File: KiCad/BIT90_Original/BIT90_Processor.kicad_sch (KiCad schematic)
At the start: 24 parts, among them SW65 RST, U1 D4016, U13 74LS138, U14 74LS05, U2 2764, U3 2764, U4 2764, U5 Z80, U6 74LS74, U8 74LS32

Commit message: Completed original schematic redraw
Well, didn't finish the Video Encoder (PAL) sheet as I'm not going to use any of it in the new design.
Moved the audio output from that sheet to the Joystick/Audio/Tape out sheet where the sound generator is.
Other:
- moved on the sheet: C15, C76, D2, D3, D4, R1, R10, R11, R21, R22, R35, R39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

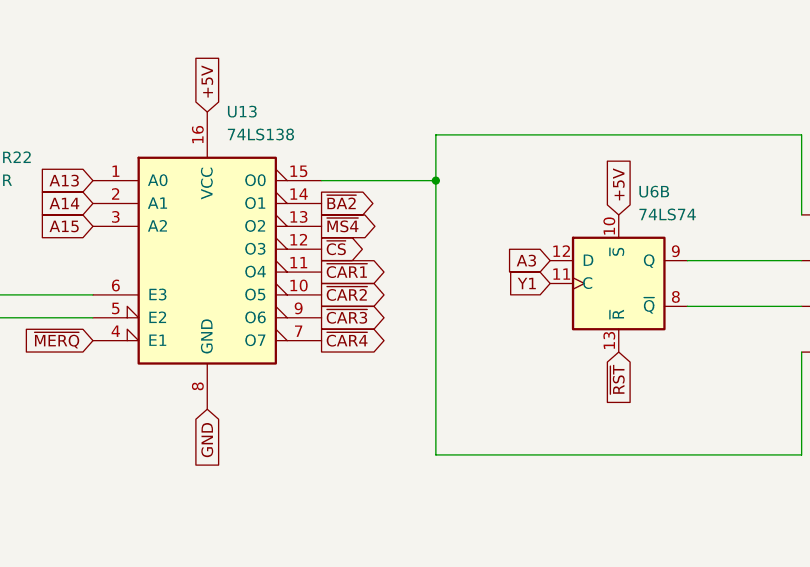
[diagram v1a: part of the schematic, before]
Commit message: Small updates/corrections
Managed to figure out some more errors/missing info from ColecoVision schematics & Henk's BIT90 motherboard underside photo
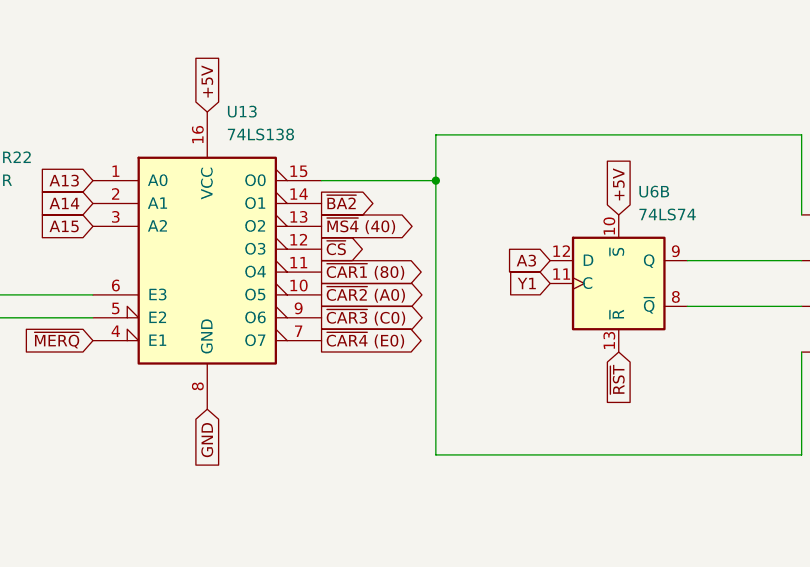
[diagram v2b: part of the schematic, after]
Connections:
- net ~{CAR1} renamed ~{CAR1} (80)
- net ~{CAR2} renamed ~{CAR2} (A0)
- net ~{CAR3} renamed ~{CAR3} (C0)
- net ~{CAR4} renamed ~{CAR4} (E0)
- net ~{MS4} renamed ~{MS4} (40)
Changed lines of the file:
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@@
 	(title_block
 		(title "BIT90 Processor")
-		(date "4/JUN/2026")
+		(date "5/JUN/2026")
 		(rev "A")
 		(company "Brett Hallen")
@@
 		)
 	)
-	(global_label "~{CAR1}"
+	(global_label "~{CAR1} (80)"
 		(shape output)
 		(at 102.87 57.15 0)
@@
 		)
 	)
-	(global_label "~{CAR3}"
+	(global_label "~{CAR3} (C0)"
 		(shape output)
 		(at 102.87 62.23 0)
@@
 		)
 	)
-	(global_label "~{MS4}"
+	(global_label "~{MS4} (40)"
 		(shape output)
 		(at 102.87 52.07 0)
@@
 		)
 	)
-	(global_label "~{CAR2}"
+	(global_label "~{CAR2} (A0)"
 		(shape output)
 		(at 102.87 59.69 0)
@@
 		)
 	)
-	(global_label "~{CAR4}"
+	(global_label "~{CAR4} (E0)"
 		(shape output)
 		(at 102.87 64.77 0)

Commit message: Resolved audio clock signal
Marked as EXTΦ on BIT90 schematic, generated via resistor from CPUΦ
Renamed it as AUDΦ so it's a bit clearer
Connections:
- net ~{CAR1} (80) renamed ~{CAR1}_(80)
- net ~{CAR2} (A0) renamed ~{CAR2}_(A0)
- net ~{CAR3} (C0) renamed ~{CAR3}_(C0)
- net ~{CAR4} (E0) renamed ~{CAR4}_(E0)
- net ~{MS4} (40) renamed ~{MS4}_(40)
